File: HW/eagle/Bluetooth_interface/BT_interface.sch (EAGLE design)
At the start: 30 parts, among them IC3 FT232RL, IC5 UA78M05DCY

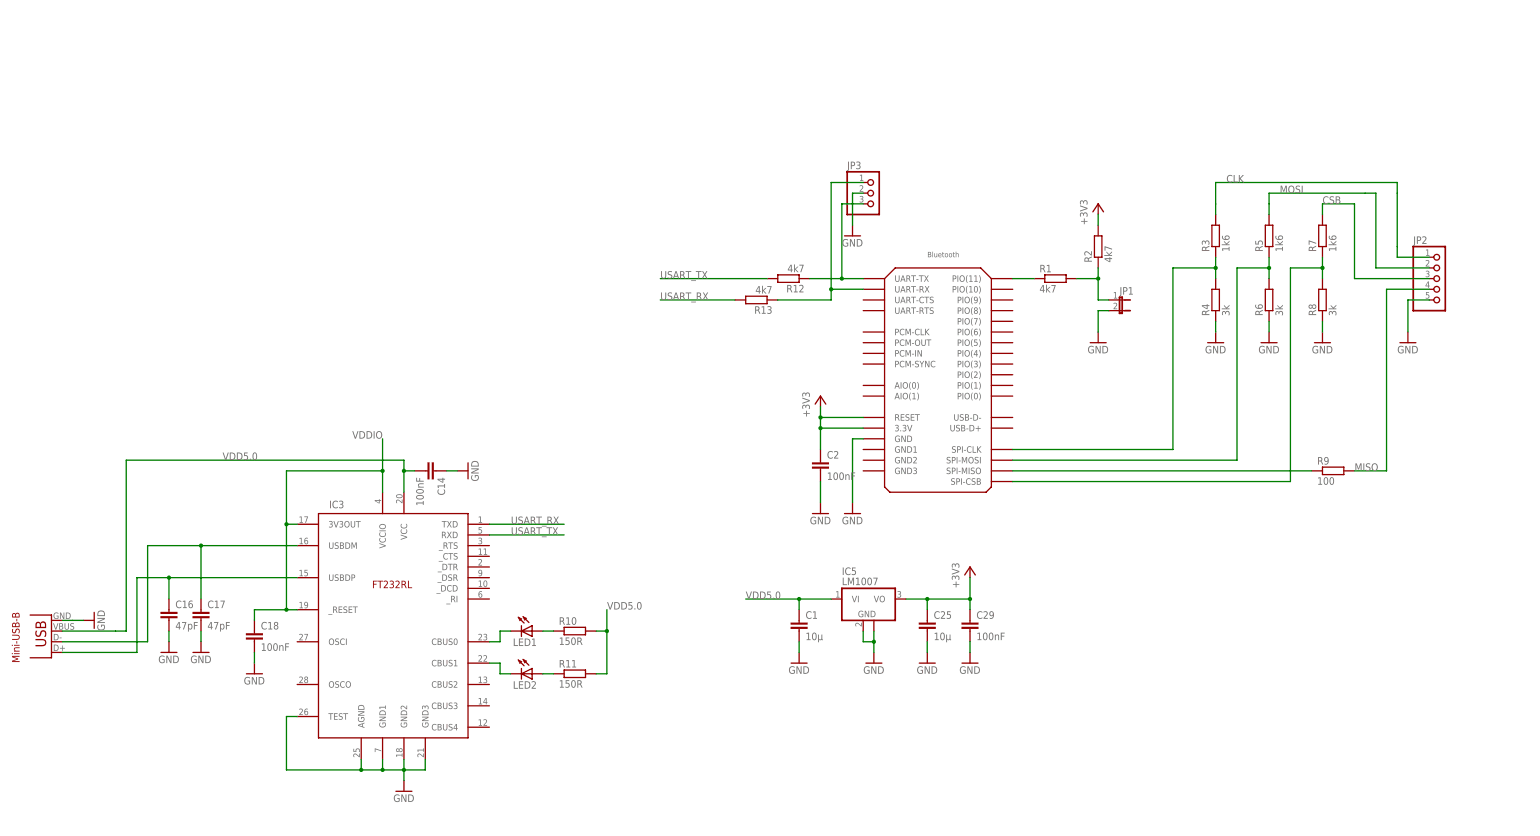
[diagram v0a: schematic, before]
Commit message: labels changed, parts smashed, labels resized and rearranged
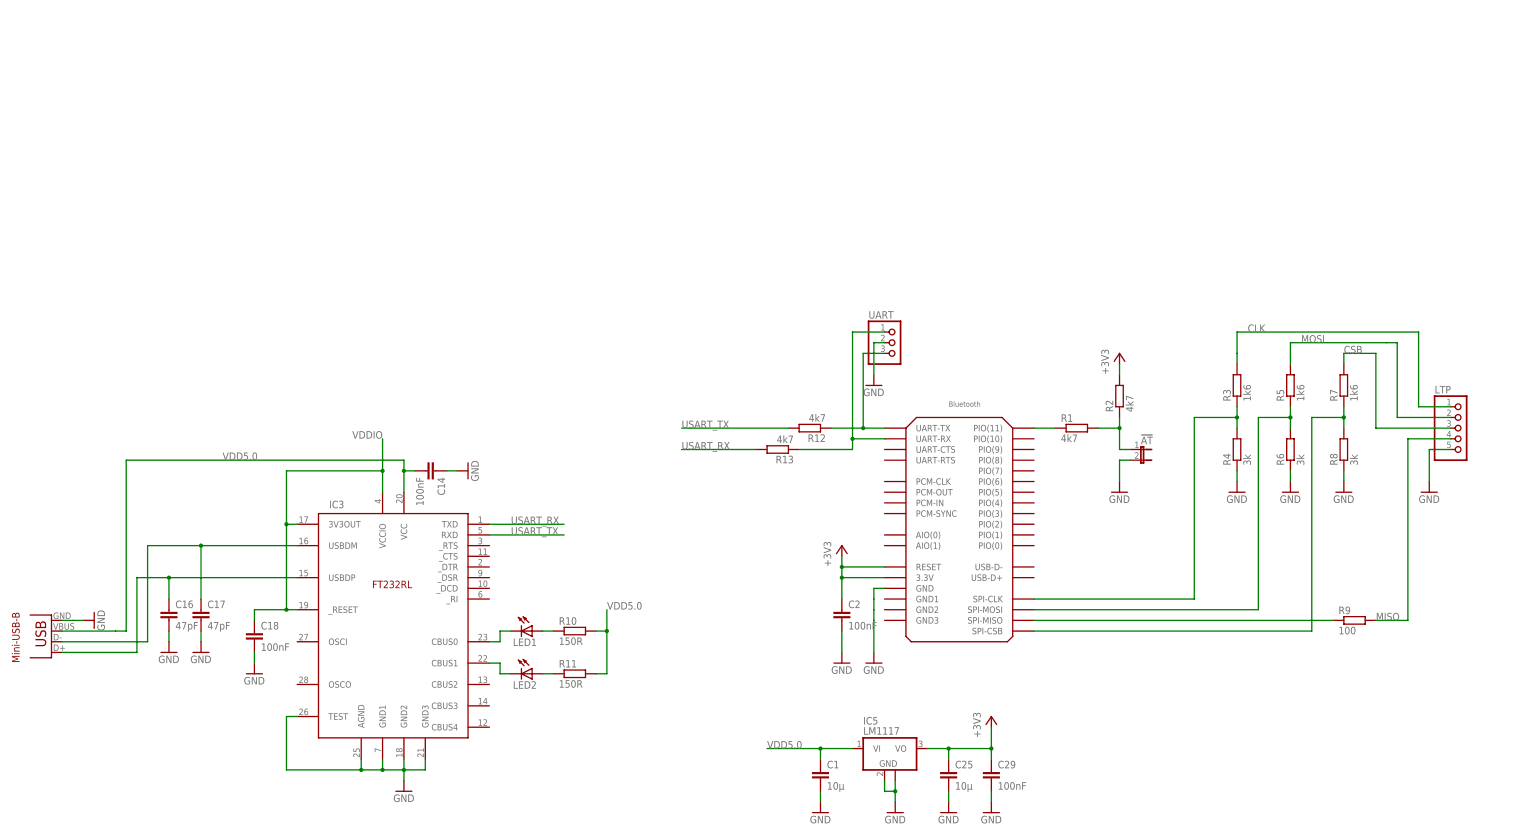
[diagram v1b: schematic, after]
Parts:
- removed JP1: (no value), daGloane:JUMPER-2PTH
- removed JP2: (no value), pinhead:PINHD-1X5
- removed JP3: (no value), pinhead:PINHD-1X3
- added !AT: (no value), daGloane:JUMPER-2PTH
- added LTP: (no value), pinhead:PINHD-1X5
- added UART: (no value), pinhead:PINHD-1X3
- IC5: LM1007 LM1007 -> (none); LM1117 (none) -> LM1117
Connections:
- net CLK: now also LTP.1; no longer JP2.1
- net CSB: now also LTP.3; no longer JP2.3
- net GND: now also !AT.2, LTP.5, UART.2; no longer JP1.2, JP2.5, JP3.2
- net MISO: now also LTP.4; no longer JP2.4
- net MOSI: now also LTP.2; no longer JP2.2
- net N$10: now also UART.3; no longer JP3.3
- net N$11: now also UART.1; no longer JP3.1
- net N$6: now also !AT.1; no longer JP1.1
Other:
- moved on the sheet: C1, C2, C25, C29, IC5, R1, R12, R13, R2, R3, R4, R5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

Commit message: layout finished
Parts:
- added U$10, U$11, U$2, U$3, U$4, U$5, U$6, U$7, U$8, U$9: SPRING_HEADER, daGloane:SPRING_HEADER
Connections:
- net +3V3: now also U$4.TP, U$5.TP
- net CLK: now also LTP.3; no longer LTP.1
- net CSB: now also LTP.5; no longer LTP.3
- net GND: now also LTP.1, U$6.TP; no longer LTP.5
- net MISO: now also LTP.2; no longer LTP.4
- net MOSI: now also LTP.4; no longer LTP.2
- net N$1: now also U$9.TP
- net N$10: now also U$2.TP
- net N$11: now also U$3.TP
- net N$15: now also U$10.TP
- net N$7: now also U$11.TP
- net N$8: now also U$7.TP
- net N$9: now also U$8.TP

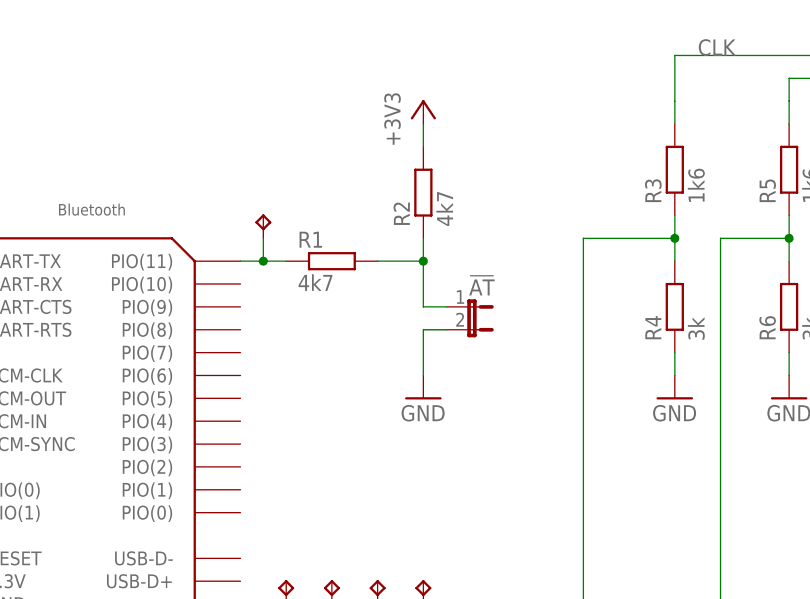
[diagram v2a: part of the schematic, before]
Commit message: added status LED
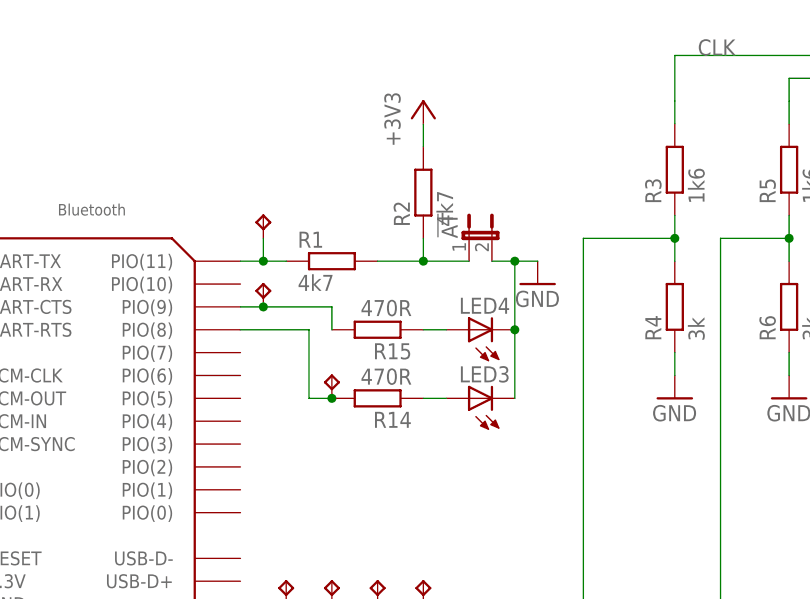
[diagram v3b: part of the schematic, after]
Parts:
- added LED3, LED4: (no value), led:LEDCHIPLED_0603
- added R14, R15: 470R, rcl:R-EU_R0805
- added U$12, U$13: SPRING_HEADER, daGloane:SPRING_HEADER
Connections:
- new net N$12: LED3.A, R14.1
- new net N$13: LED4.A, R15.1
- new net N$14: R14.2, U$1.PIO(8), U$13.TP
- new net N$16: R15.2, U$1.PIO(9), U$12.TP
- net GND: now also LED3.C, LED4.C
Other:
- moved on the sheet: ~{AT}
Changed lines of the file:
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@@
 <?xml version="1.0" encoding="utf-8"?>
 <!DOCTYPE eagle SYSTEM "eagle.dtd">
-<eagle version="6.1">
+<eagle version="6.2">
 <drawing>
 <settings>
@@
 <part name="U$8" library="daGloane" deviceset="SPRING_HEADER" device=""/>
 <part name="U$9" library="daGloane" deviceset="SPRING_HEADER" device=""/>
+<part name="R14" library="rcl" deviceset="R-EU_" device="R0805" value="470R"/>
+<part name="R15" library="rcl" deviceset="R-EU_" device="R0805" value="470R"/>
+<part name="LED3" library="led" deviceset="LED" device="CHIPLED_0603"/>
+<part name="LED4" library="led" deviceset="LED" device="CHIPLED_0603"/>
+<part name="U$12" library="daGloane" deviceset="SPRING_HEADER" device=""/>
+<part name="U$13" library="daGloane" deviceset="SPRING_HEADER" device=""/>
 </parts>
 <sheets>
@@
 <instance part="C2" gate="G$1" x="208.28" y="66.04"/>
 <instance part="GND3" gate="1" x="208.28" y="53.34"/>
-<instance part="!AT" gate="A" x="279.4" y="104.14" rot="R270"/>
+<instance part="!AT" gate="A" x="279.4" y="111.76"/>
 <instance part="R1" gate="G$1" x="264.16" y="109.22"/>
 <instance part="R2" gate="G$1" x="274.32" y="116.84" rot="R90"/>
-<instance part="GND4" gate="1" x="274.32" y="93.98"/>
+<instance part="GND4" gate="1" x="287.02" y="106.68"/>
 <instance part="+3V3" gate="G$1" x="274.32" y="127"/>
 <instance part="R3" gate="G$1" x="302.26" y="119.38" rot="R90"/>
@@
 <instance part="U$8" gate="G$1" x="259.08" y="73.66" smashed="yes"/>
 <instance part="U$9" gate="G$1" x="256.54" y="114.3" smashed="yes"/>
+<instance part="R14" gate="G$1" x="269.24" y="93.98" rot="R180"/>
+<instance part="R15" gate="G$1" x="269.24" y="101.6" rot="R180"/>
+<instance part="LED3" gate="G$1" x="279.4" y="93.98" rot="R90"/>
+<instance part="LED4" gate="G$1" x="279.4" y="101.6" rot="R90"/>
+<instance part="U$12" gate="G$1" x="256.54" y="106.68" smashed="yes"/>
+<instance part="U$13" gate="G$1" x="264.16" y="96.52" smashed="yes"/>
 </instances>
 <busses>
@@
 <segment>
 <pinref part="GND4" gate="1" pin="GND"/>
-<wire x1="274.32" y1="96.52" x2="274.32" y2="101.6" width="0.1524" layer="91"/>
 <pinref part="!AT" gate="A" pin="2"/>
-<wire x1="274.32" y1="101.6" x2="276.86" y2="101.6" width="0.1524" layer="91"/>
+<wire x1="287.02" y1="109.22" x2="284.48" y2="109.22" width="0.1524" layer="91"/>
+<pinref part="LED3" gate="G$1" pin="C"/>
+<pinref part="LED4" gate="G$1" pin="C"/>
+<wire x1="284.48" y1="109.22" x2="281.94" y2="109.22" width="0.1524" layer="91"/>
+<wire x1="284.48" y1="93.98" x2="284.48" y2="101.6" width="0.1524" layer="91"/>
+<wire x1="284.48" y1="101.6" x2="284.48" y2="109.22" width="0.1524" layer="91"/>
+<junction x="284.48" y="101.6"/>
+<junction x="284.48" y="109.22"/>
 </segment>
 <segment>
@@
 <wire x1="274.32" y1="109.22" x2="274.32" y2="111.76" width="0.1524" layer="91"/>
 <pinref part="!AT" gate="A" pin="1"/>
-<wire x1="276.86" y1="104.14" x2="274.32" y2="104.14" width="0.1524" layer="91"/>
-<wire x1="274.32" y1="104.14" x2="274.32" y2="109.22" width="0.1524" layer="91"/>
+<wire x1="279.4" y1="109.22" x2="274.32" y2="109.22" width="0.1524" layer="91"/>
 <junction x="274.32" y="109.22"/>
 </segment>
@@
 </segment>
 </net>
+<net name="N$12" class="0">
+<segment>
+<wire x1="274.32" y1="93.98" x2="276.86" y2="93.98" width="0.1524" layer="91"/>
+<pinref part="R14" gate="G$1" pin="1"/>
+<pinref part="LED3" gate="G$1" pin="A"/>
+</segment>
+</net>
+<net name="N$13" class="0">
+<segment>
+<wire x1="274.32" y1="101.6" x2="276.86" y2="101.6" width="0.1524" layer="91"/>
+<pinref part="R15" gate="G$1" pin="1"/>
+<pinref part="LED4" gate="G$1" pin="A"/>
+</segment>
+</net>
+<net name="N$14" class="0">
+<segment>
+<pinref part="U$1" gate="G$1" pin="PIO(8)"/>
+<wire x1="254" y1="101.6" x2="261.62" y2="101.6" width="0.1524" layer="91"/>
+<wire x1="261.62" y1="101.6" x2="261.62" y2="93.98" width="0.1524" layer="91"/>
+<pinref part="R14" gate="G$1" pin="2"/>
+<wire x1="261.62" y1="93.98" x2="264.16" y2="93.98" width="0.1524" layer="91"/>
+<pinref part="U$13" gate="G$1" pin="TP"/>
+<junction x="264.16" y="93.98"/>
+</segment>
+</net>
+<net name="N$16" class="0">
+<segment>
+<pinref part="U$1" gate="G$1" pin="PIO(9)"/>
+<pinref part="R15" gate="G$1" pin="2"/>
+<wire x1="254" y1="104.14" x2="256.54" y2="104.14" width="0.1524" layer="91"/>
+<wire x1="256.54" y1="104.14" x2="264.16" y2="104.14" width="0.1524" layer="91"/>
+<wire x1="264.16" y1="104.14" x2="264.16" y2="101.6" width="0.1524" layer="91"/>
+<pinref part="U$12" gate="G$1" pin="TP"/>
+<junction x="256.54" y="104.14"/>
+</segment>
+</net>

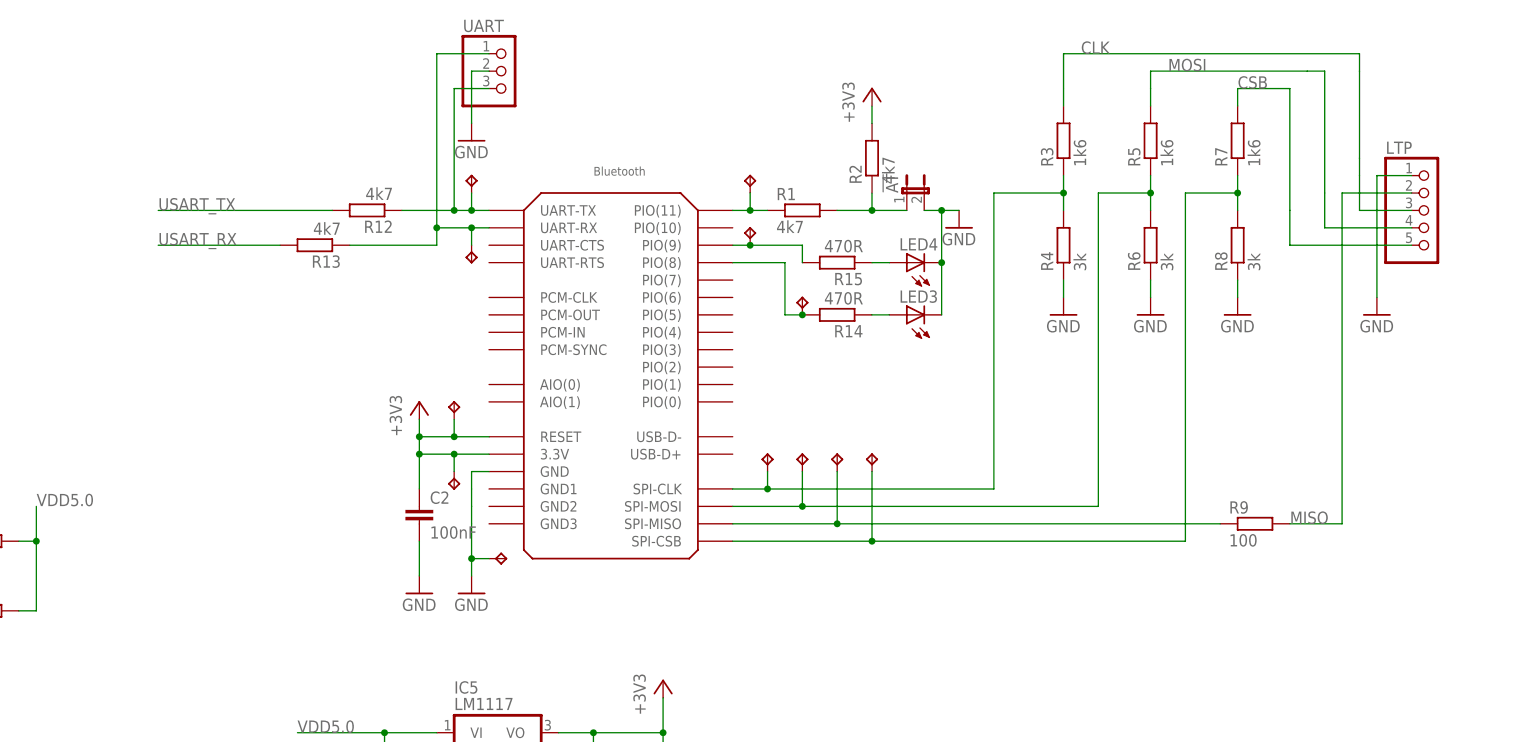
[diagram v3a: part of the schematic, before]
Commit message: parts rearranged to leave more space for BT module
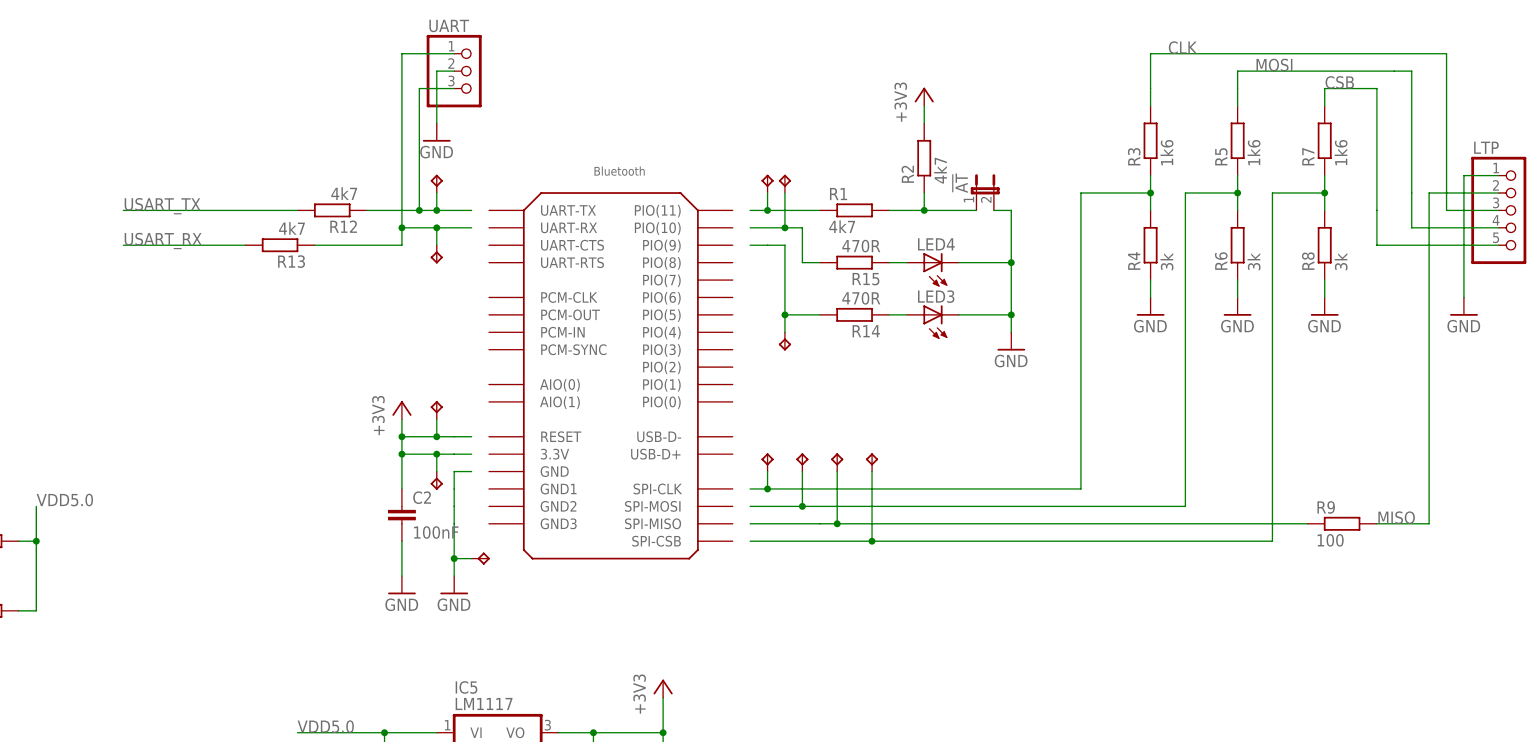
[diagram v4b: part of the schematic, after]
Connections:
- net +3V3: no longer U$1.3.3V, U$1.RESET
- net GND: no longer U$1.GND
- net N$1: no longer U$1.PIO(11)
- net N$10: no longer U$1.UART-TX
- net N$11: no longer U$1.UART-RX
- net N$14: no longer U$1.PIO(8)
- net N$15: no longer U$1.SPI-MISO
- net N$16: no longer U$1.PIO(9)
- net N$7: no longer U$1.SPI-CSB
- net N$8: no longer U$1.SPI-MOSI
- net N$9: no longer U$1.SPI-CLK
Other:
- moved on the sheet: C2, LED3, LED4, LTP, R1, R12, R13, R14, R15, R2, R3, R4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
